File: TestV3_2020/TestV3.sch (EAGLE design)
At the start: 116 parts, among them J11 CONN_03, J4 XT30UPB-F, J5 CONN_03, J6 XT30UPB-F, Q3 600mA/40V, Q4 600mA/40V, U2 MP2451, U4 LIGHT_SENSORALS

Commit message: finished all the board layouts
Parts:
- removed 3C4: 1000uF, JH:1000UF-CAP
- removed C3: 100uF, SparkFun-Capacitors:100UF-POLAR-10X10.5-63V-20%
- added 3C5: 0.1uF, JH:CAPACITOR0603
- added JP1: JUMPER-SMT_2_NO_NO-SILK_ROUND, SparkFun-Jumpers:JUMPER-SMT_2_NO_NO-SILK_ROUND
- 3C3: value 0.1uF -> 100uF; device JH:CAPACITOR0603 -> SparkFun-Capacitors:100UF-POLAR-10X10.5-63V-20%
- renumbered POT1 to 3POT1, R13 to 3R3, R18 to 3R4
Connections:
- net GND-BOOST: now also 3C3.-, JP1.1; no longer 3C4.-, C3.-
- net GND-CS: now also J1.2; no longer J1.1
- net GND-POT: now also 3C5.2, J2.2, JP1.2; no longer 3C3.2, J2.1
- net VIN-CS: now also J1.1; no longer J1.2
- net VIN-POT: now also 3C5.1, J2.1; no longer 3C3.1, J2.2
- net VOUT-BOOST: now also 3C3.+; no longer 3C4.+, C3.+

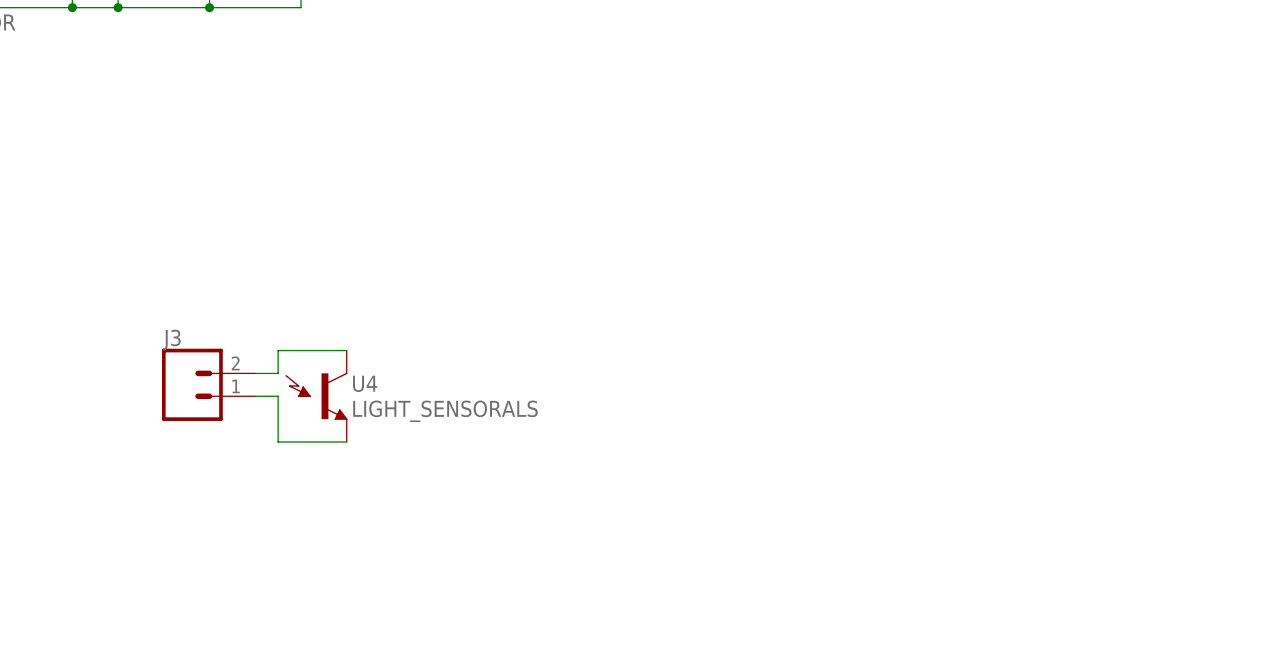
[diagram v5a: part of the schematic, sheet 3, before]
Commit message: added more light sensors and lights to test and optimise positioning, added xt60 for test fitting
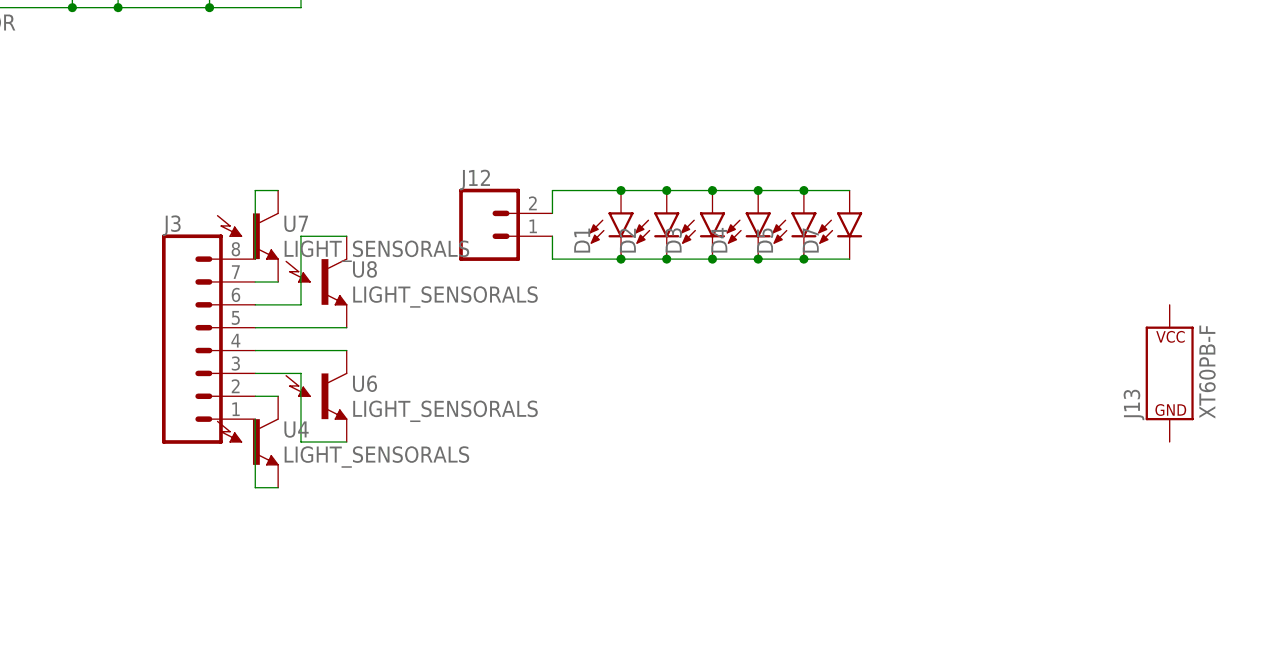
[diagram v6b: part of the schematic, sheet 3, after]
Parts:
- added D1, D2, D3, D4, D5, D7: 3528LED, JH:3528LED
- added J12: (no value), SparkFun-Connectors:CONN_02LOCK
- added J13: XT60PB-F, JH:XT60PB-F
- added U6, U7, U8: LIGHT_SENSORALS, SparkFun-Sensors:LIGHT_SENSORALS
- J3: device SparkFun-Connectors:CONN_02LOCK -> SparkFun-Connectors:CONN_08LOCK
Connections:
- new net N$19: J3.4, U6.C1
- new net N$56: J3.3, U6.E1
- new net N$61: J3.8, U7.C1
- new net N$62: J3.7, U7.E1
- new net N$63: J3.5, U8.E1
- new net N$64: J3.6, U8.C1
- new net N$7: D1.A, D2.A, D3.A, D4.A, D5.A, D7.A, J12.2
- net N$13: now also D1.C, D2.C, D3.C, D4.C, D5.C, D7.C, J12.1; no longer 1C5.1, 1U2.IN
- net V_USB: now also 1C5.1, 1U2.IN
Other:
- moved on the sheet: U4

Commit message: minor changes, mostly fixed the values of some components
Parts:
- 3R4: value 45k -> 47k
- 4C11: value 4.7nF -> 4700pF
- R28: value 20k-75k -> 47k
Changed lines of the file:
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@@
 <part name="4JP2" library="SparkFun-Jumpers" library_urn="urn:adsk.eagle:library:528" deviceset="JUMPER-SMT_3_NO" device="_NO-SILK" package3d_urn="urn:adsk.eagle:package:39284/1" value="JUMPER-SMT_3_NO_NO-SILK"/>
 <part name="4R5" library="JH" library_urn="urn:adsk.eagle:library:6027132" deviceset="RESISTOR" device="0603" package3d_urn="urn:adsk.eagle:package:15441228/3" value="49.9k"/>
-<part name="4C11" library="JH" library_urn="urn:adsk.eagle:library:6027132" deviceset="CAPACITOR" device="0603" package3d_urn="urn:adsk.eagle:package:15441226/3" value="4.7nF"/>
+<part name="4C11" library="JH" library_urn="urn:adsk.eagle:library:6027132" deviceset="CAPACITOR" device="0603" package3d_urn="urn:adsk.eagle:package:15441226/3" value="4700pF"/>
 <part name="4C12" library="JH" library_urn="urn:adsk.eagle:library:6027132" deviceset="CAPACITOR" device="0603" package3d_urn="urn:adsk.eagle:package:15441226/3" value="39pF"/>
 <part name="4R7" library="JH" library_urn="urn:adsk.eagle:library:6027132" deviceset="RESISTOR" device="0603" package3d_urn="urn:adsk.eagle:package:15441228/3" value="1.91k"/>
@@
 <part name="3D1" library="diode" library_urn="urn:adsk.eagle:library:210" deviceset="SCHOTTKY-DIODE" device="SMD" package3d_urn="urn:adsk.eagle:package:43404/2" value="SS510"/>
 <part name="3POT1" library="JH" library_urn="urn:adsk.eagle:library:6027132" deviceset="3296-TRIMPOT" device="" package3d_urn="urn:adsk.eagle:package:15850924/1" value="10k"/>
-<part name="3R4" library="JH" library_urn="urn:adsk.eagle:library:6027132" deviceset="RESISTOR" device="0603" package3d_urn="urn:adsk.eagle:package:15441228/3" value="45k"/>
+<part name="3R4" library="JH" library_urn="urn:adsk.eagle:library:6027132" deviceset="RESISTOR" device="0603" package3d_urn="urn:adsk.eagle:package:15441228/3" value="47k"/>
 <part name="3C3" library="SparkFun-Capacitors" library_urn="urn:adsk.eagle:library:510" deviceset="100UF-POLAR" device="-10X10.5-63V-20%" package3d_urn="urn:adsk.eagle:package:37417/1" value="100uF"/>
 <part name="3C5" library="JH" library_urn="urn:adsk.eagle:library:6027132" deviceset="CAPACITOR" device="0603" package3d_urn="urn:adsk.eagle:package:15441226/3" value="0.1uF"/>
@@
 <attribute name="VOLTAGE" value="16V"/>
 </part>
-<part name="R28" library="JH" library_urn="urn:adsk.eagle:library:6027132" deviceset="RESISTOR" device="0603" package3d_urn="urn:adsk.eagle:package:15441228/3" value="20k-75k"/>
+<part name="R28" library="JH" library_urn="urn:adsk.eagle:library:6027132" deviceset="RESISTOR" device="0603" package3d_urn="urn:adsk.eagle:package:15441228/3" value="47k"/>
 <part name="R29" library="JH" library_urn="urn:adsk.eagle:library:6027132" deviceset="RESISTOR" device="0603" package3d_urn="urn:adsk.eagle:package:15441228/3" value="100k"/>
 <part name="J4" library="JH" library_urn="urn:adsk.eagle:library:6027132" deviceset="XT30UPB-F" device="" package3d_urn="urn:adsk.eagle:package:15925142/1"/>
